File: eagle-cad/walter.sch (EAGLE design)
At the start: 14 parts, among them U1 LP38511MRX-ADJ/NOPB

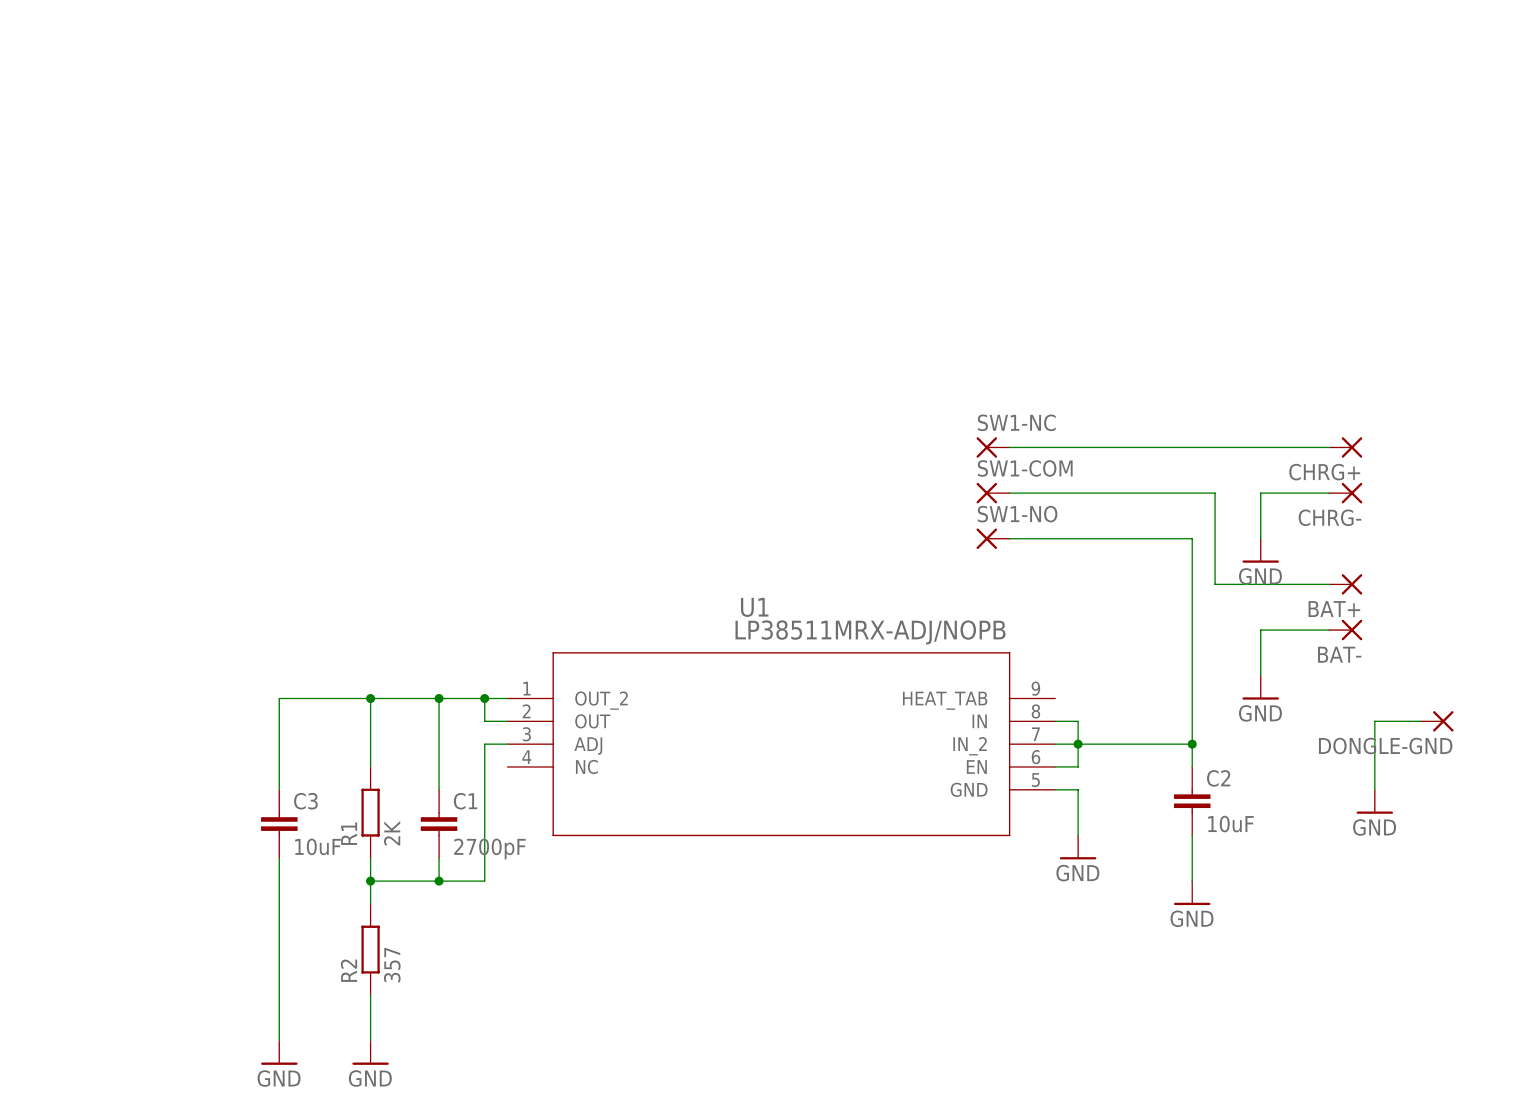
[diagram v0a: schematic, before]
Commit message: schematics update
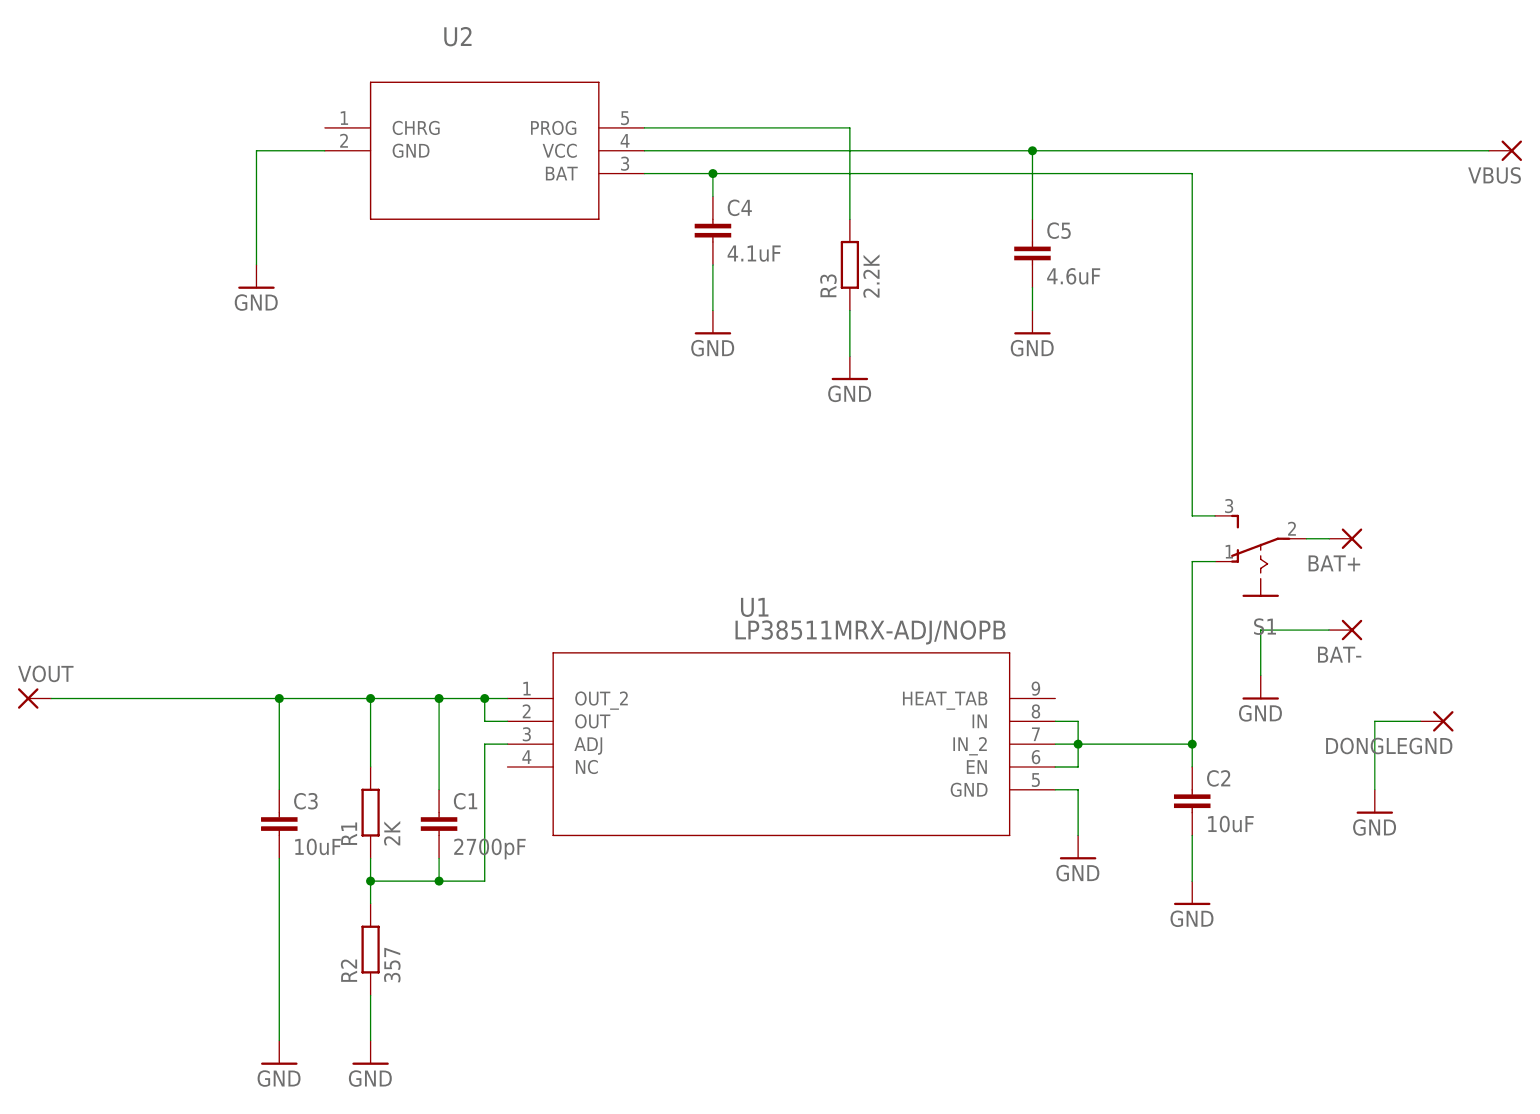
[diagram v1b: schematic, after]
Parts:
- removed CHRG+, CHRG-, DONGLE-GND, SW1-COM, SW1-NC, SW1-NO: (no value), wirepad:SMD2
- added C4: 4.1uF, rcl:C-EUC0603
- added C5: 4.6uF, rcl:C-EUC0603
- added DONGLEGND, VBUS, VOUT: (no value), wirepad:1,6/0,8
- added R3: 2.2K, rcl:R-EU_R0603
- added S1: (no value), switch:255SB
- added U2: LTC4054LES5-4.2TRPBF, LTC4054:LTC4054LES5-4.2TRPBF
- BAT+, BAT-: device wirepad:SMD2 -> wirepad:1,6/0,8
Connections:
- new net N$2: C4.1, S1.S, U2.BAT
- new net N$6: R3.2, U2.PROG
- net GND: now also C4.2, C5.2, DONGLEGND.P, R3.1, U2.GND; no longer CHRG-.P, DONGLE-GND.P
- net N$1: now also S1.O; no longer SW1-NO.P
- net N$3: now also VOUT.P
- net N$5: now also S1.P; no longer SW1-COM.P
- net N$7: now also C5.1, U2.VCC, VBUS.P; no longer CHRG+.P, SW1-NC.P
